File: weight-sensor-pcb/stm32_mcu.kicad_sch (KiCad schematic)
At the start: 6 parts, among them J1 TC2030, U4 STM32F042F4P6

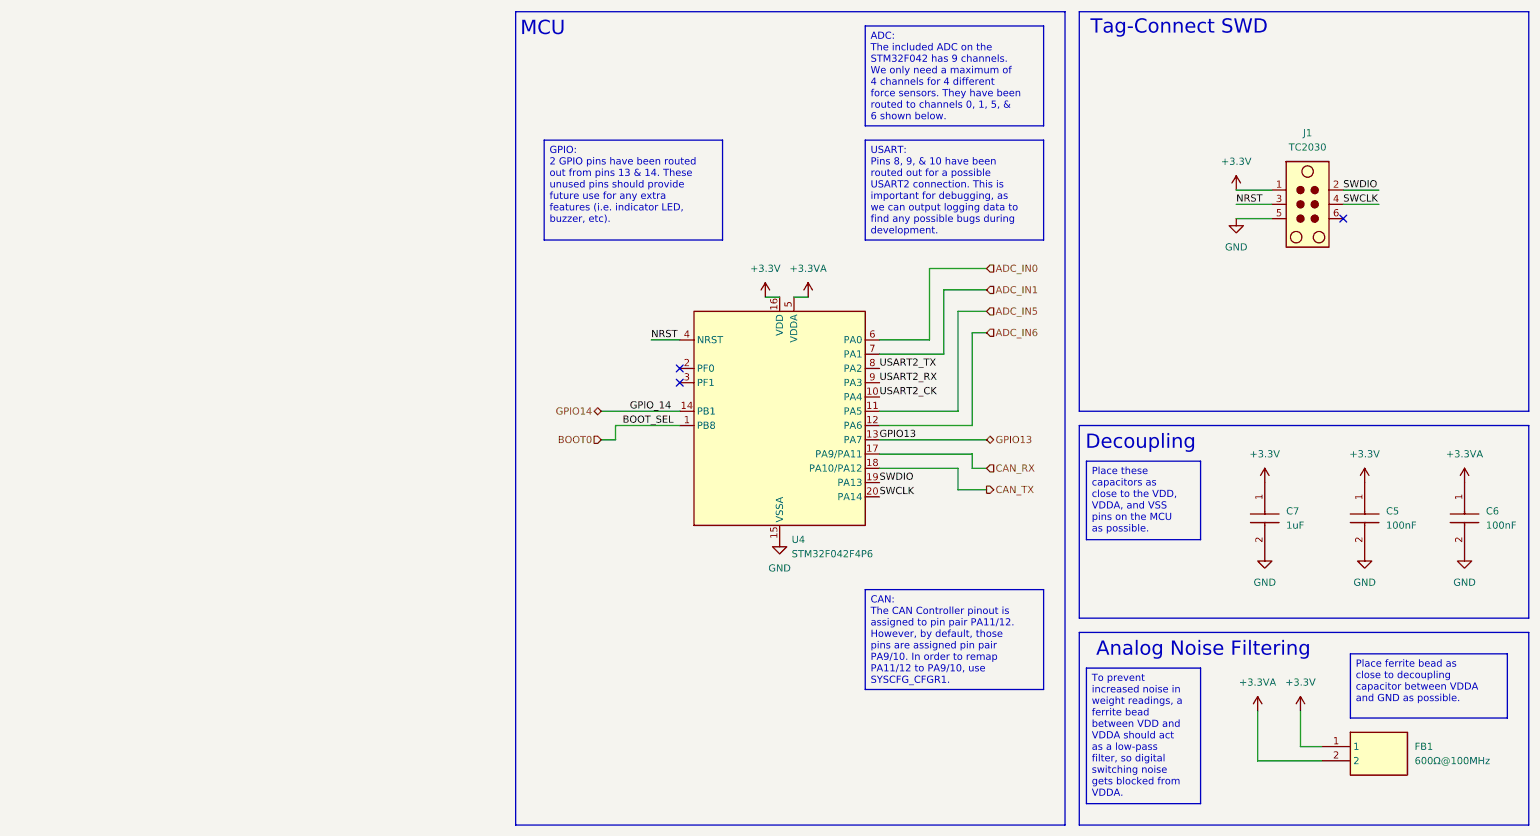
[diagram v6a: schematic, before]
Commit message: Add Test points, CAN connector, USART connector
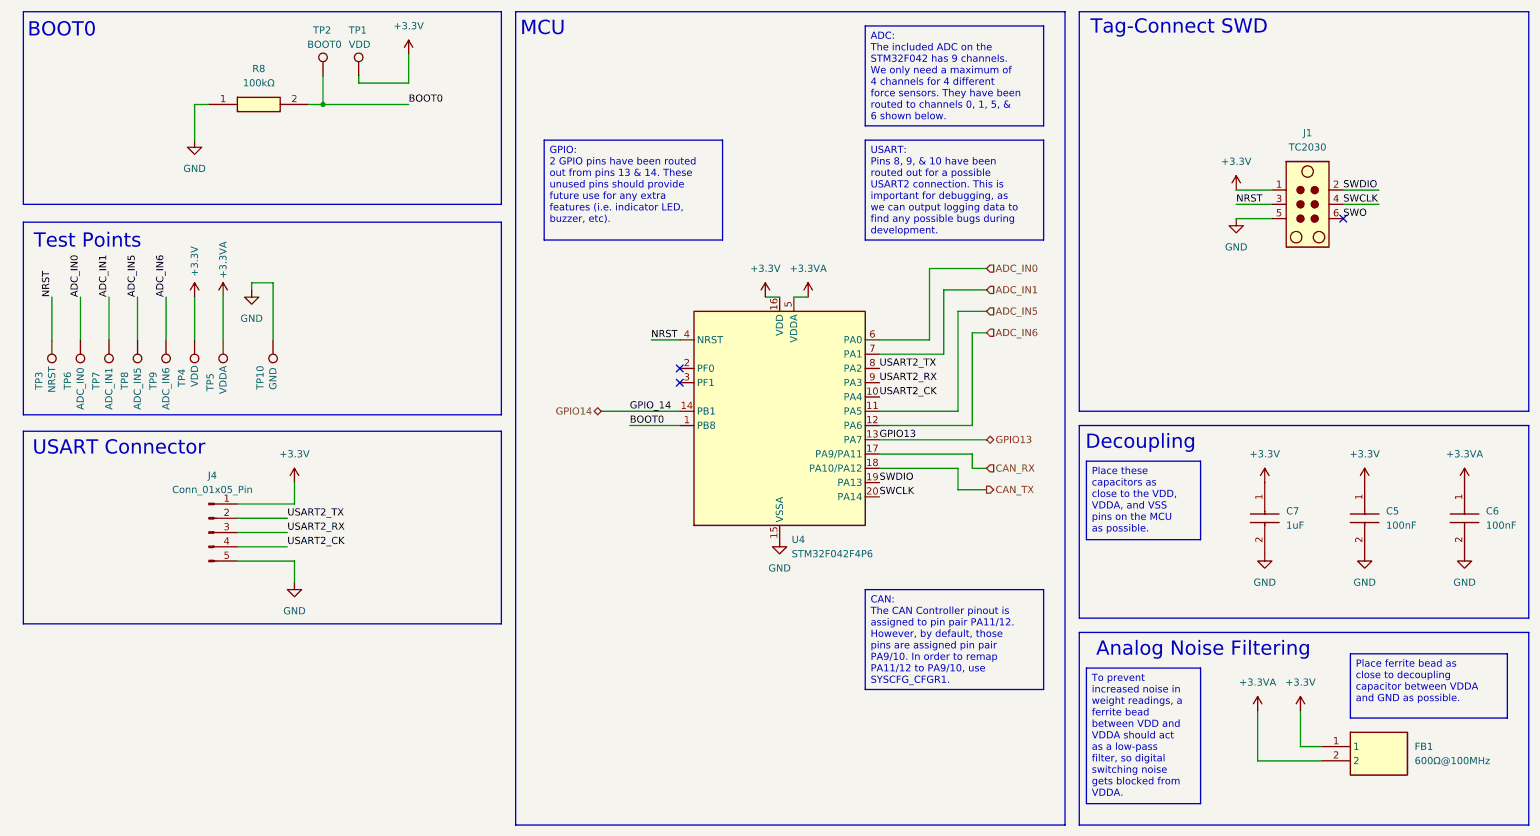
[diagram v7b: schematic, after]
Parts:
- added J4: Conn_01x05_Pin, Connector_PinHeader_1.27mm:PinHeader_1x05_P1.27mm_Vertical, symbol Connector:Conn_01x05_Pin
- added R8: 100kΩ, RESC1005X40N, symbol Capstone:RC0402FR-07100KL
- added TP1, TP4: VDD, symbol Connector:TestPoint
- added TP10: GND, symbol Connector:TestPoint
- added TP2: BOOT0, symbol Connector:TestPoint
- added TP3: NRST, symbol Connector:TestPoint
- added TP5: VDDA, symbol Connector:TestPoint
- added TP6: ADC_IN0, symbol Connector:TestPoint
- added TP7: ADC_IN1, symbol Connector:TestPoint
- added TP8: ADC_IN5, symbol Connector:TestPoint
- added TP9: ADC_IN6, symbol Connector:TestPoint
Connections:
- net +3.3V: now also J4.1 (Pin_1), TP1.1, TP4.1
- net +3.3VA: now also TP5.1
- net ADC_IN0: now also TP6.1
- net ADC_IN1: now also TP7.1
- net ADC_IN5: now also TP8.1
- net ADC_IN6: now also TP9.1
- net BOOT0: now also R8.2, TP2.1
- net GND: now also J4.5 (Pin_5), R8.1, TP10.1
- net NRST: now also TP3.1
- net USART2_CK: now also J4.4 (Pin_4)
- net USART2_RX: now also J4.3 (Pin_3)
- net USART2_TX: now also J4.2 (Pin_2)
- net SWO: now reaches J1.6
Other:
- note added: "BOOT0"
- note added: "Test Points"
- note added: "USART Connector"

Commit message: initial PCB layout design
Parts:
- TP1, TP10, TP2, TP3, TP4, TP5, TP6, TP7, TP8, TP9: footprint (none) -> TestPoint:TestPoint_Pad_D1.5mm
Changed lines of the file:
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@@
 			)
 		)
-		(property "Footprint" ""
+		(property "Footprint" "TestPoint:TestPoint_Pad_D1.5mm"
 			(at 13.97 72.39 0)
 			(effects
@@
 			)
 		)
-		(property "Footprint" ""
+		(property "Footprint" "TestPoint:TestPoint_Pad_D1.5mm"
 			(at 78.74 25.4 0)
 			(effects
@@
 			)
 		)
-		(property "Footprint" ""
+		(property "Footprint" "TestPoint:TestPoint_Pad_D1.5mm"
 			(at 34.29 72.39 0)
 			(effects
@@
 			)
 		)
-		(property "Footprint" ""
+		(property "Footprint" "TestPoint:TestPoint_Pad_D1.5mm"
 			(at 44.45 72.39 0)
 			(effects
@@
 			)
 		)
-		(property "Footprint" ""
+		(property "Footprint" "TestPoint:TestPoint_Pad_D1.5mm"
 			(at 53.34 72.39 0)
 			(effects
@@
 			)
 		)
-		(property "Footprint" ""
+		(property "Footprint" "TestPoint:TestPoint_Pad_D1.5mm"
 			(at 72.39 25.4 0)
 			(effects
@@
 			)
 		)
-		(property "Footprint" ""
+		(property "Footprint" "TestPoint:TestPoint_Pad_D1.5mm"
 			(at 24.13 72.39 0)
 			(effects
@@
 			)
 		)
-		(property "Footprint" ""
+		(property "Footprint" "TestPoint:TestPoint_Pad_D1.5mm"
 			(at 19.05 72.39 0)
 			(effects
@@
 			)
 		)
-		(property "Footprint" ""
+		(property "Footprint" "TestPoint:TestPoint_Pad_D1.5mm"
 			(at 39.37 72.39 0)
 			(effects
@@
 			)
 		)
-		(property "Footprint" ""
+		(property "Footprint" "TestPoint:TestPoint_Pad_D1.5mm"
 			(at 29.21 72.39 0)
 			(effects
